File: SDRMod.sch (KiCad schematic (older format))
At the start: 46 parts, among them P1 CONN_02X06, Q1 Q_NPN_BCE, U1 AX5043, U2 74LVC125, U3 74LVC125, Y1 Crystal

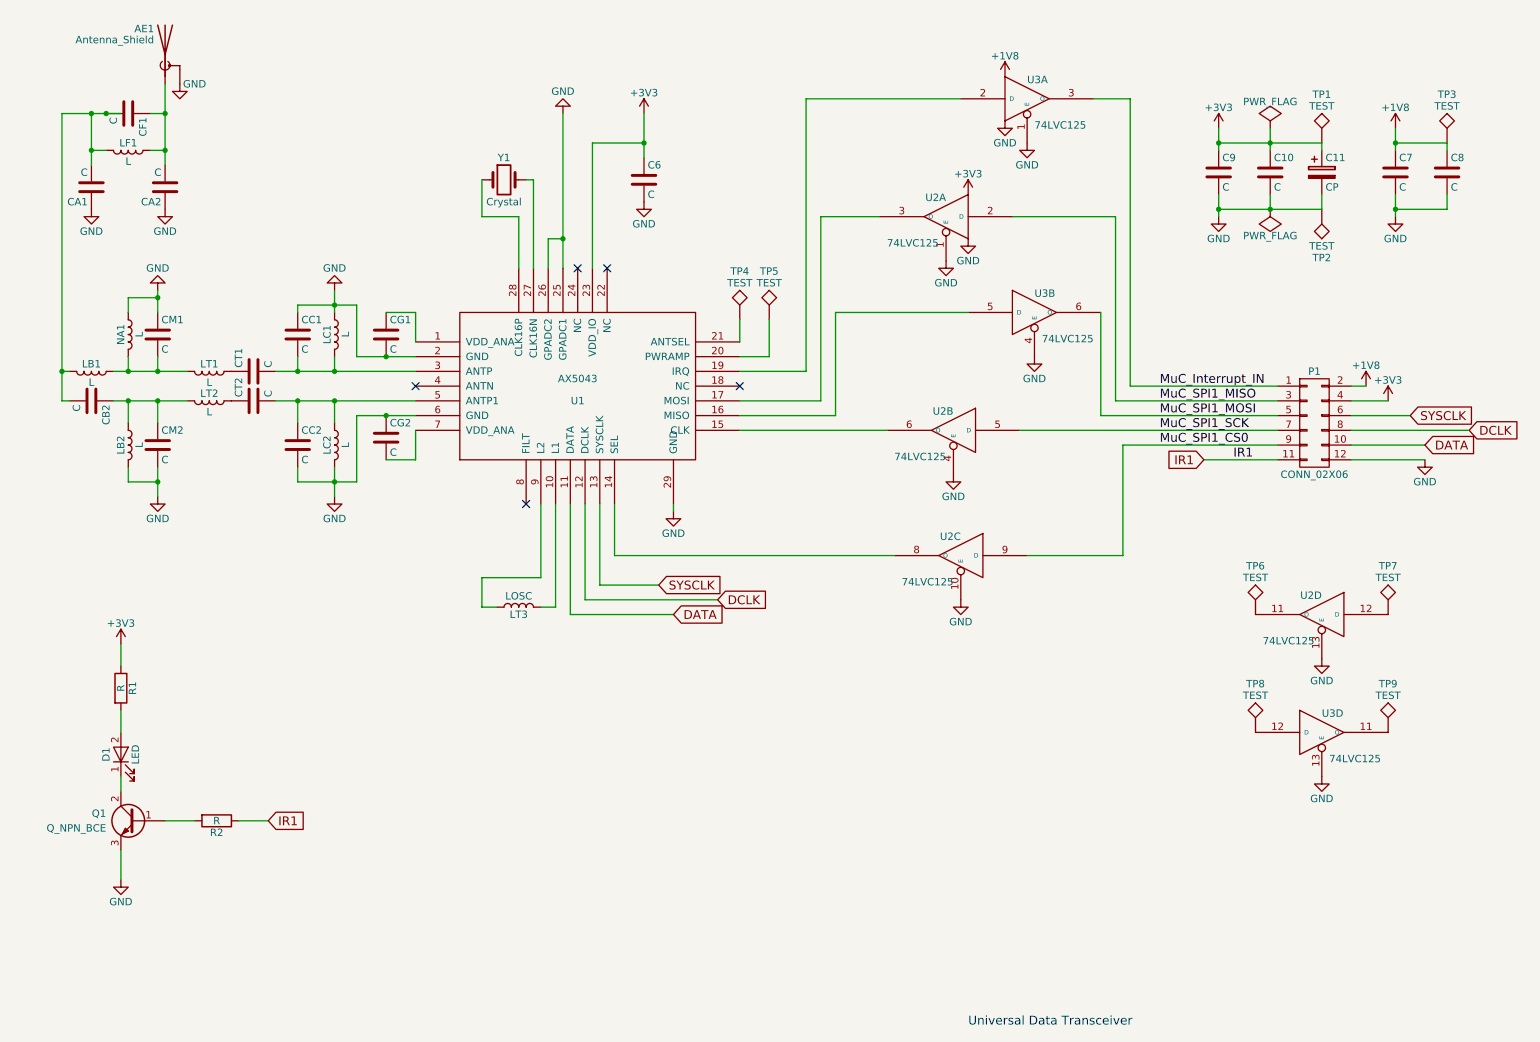
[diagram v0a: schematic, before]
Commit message: the correct project uploaded (with FET based level shifters)
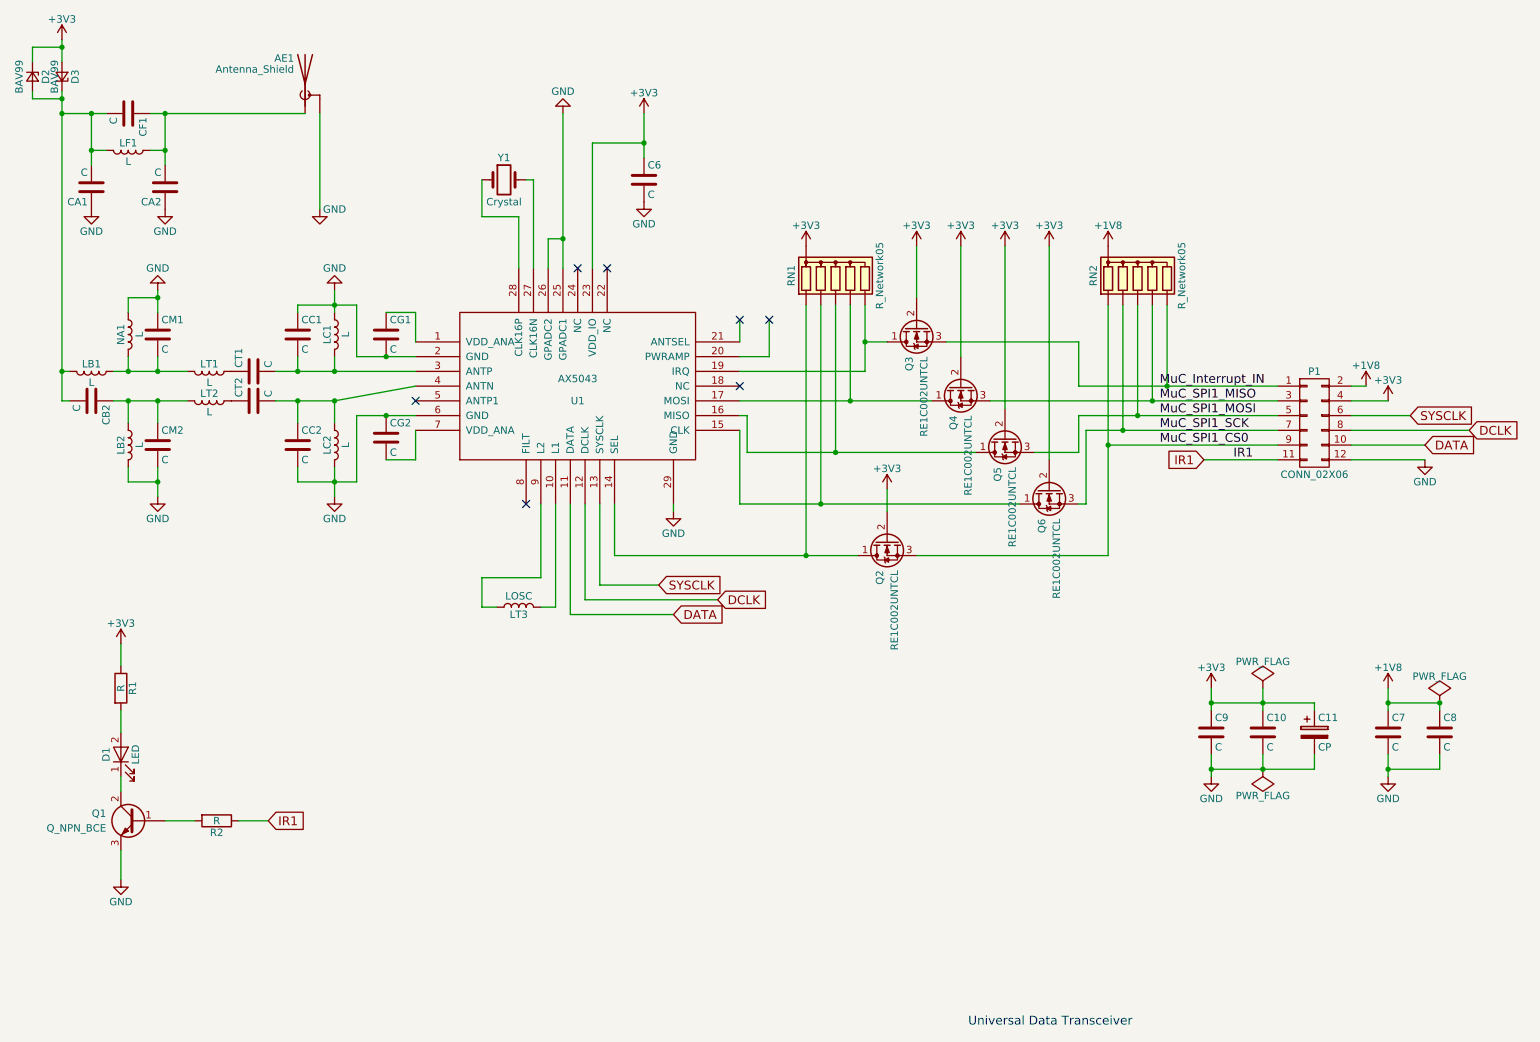
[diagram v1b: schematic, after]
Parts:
- removed TP1, TP2, TP3, TP4, TP5, TP6, TP7, TP8, TP9: TEST, Measurement_Points:Measurement_Point_Round-SMD-Pad_Small, symbol TEST
- removed U2, U3: 74LVC125, Housings_SOIC:SOIC-14_3.9x8.7mm_Pitch1.27mm, symbol 74LVC125
- added D2, D3: BAV99, Diodes_SMD:D_SCD80_HandSoldering, symbol D_Zener_Small
- added Q2, Q3, Q4, Q5, Q6: RE1C002UNTCL, TO_SOT_Packages_SMD:SOT-23_Handsoldering, symbol Q_NMOS_DGS
- added RN1, RN2: R_Network05, TO_SOT_Packages_SMD:SOT-23-6_Handsoldering, symbol R_Network05
- AE1: footprint Wire_Connections_Bridges:WireConnection_1.00mmDrill -> Connectors:SMB_Straight
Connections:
- net +1V8: now also RN2.1 (common); no longer C10.1, C11.1, C6.1, C9.1, P1.4 (P4), R1.1, U1.23 (VDD_IO)
- net MuC_Interrupt_IN: now also Q3.3 (S), RN2.6 (R5)
- net MuC_SPI1_CS0: now also Q2.3 (S), RN2.2 (R1)
- net MuC_SPI1_MISO: now also Q4.3 (S), RN2.5 (R4)
- net MuC_SPI1_MOSI: now also Q5.3 (S), RN2.4 (R3)
- net MuC_SPI1_SCK: now also Q6.3 (S), RN2.3 (R2)
- net at U1.14 (SEL): now also Q2.1 (D), RN1.2 (R1)
- net at U1.15 (CLK): now also Q6.1 (D), RN1.3 (R2)
- net at U1.16 (MISO): now also Q5.1 (D), RN1.4 (R3)
- net at U1.17 (MOSI): now also Q4.1 (D), RN1.5 (R4)
- net at U1.19 (IRQ): now also Q3.1 (D), RN1.6 (R5)
- net at U1.4 (ANTN): now also CC2.1, CT2.2, LC2.1
- net at CA1.2, CB2.2, CF1.2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: now also D2.2 (A), D3.1 (K)
- new net +3V3: C10.1, C11.1, C6.1, C9.1, D2.1 (K), D3.2 (A), P1.4 (P4), Q2.2 (G), Q3.2 (G), Q4.2 (G), Q5.2 (G), Q6.2 (G), R1.1, RN1.1 (common), U1.23 (VDD_IO)
- now unconnected: U1.5 (ANTP1)
- no-connect marks 5 -> 7
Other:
- moved on the sheet: AE1, C10, C11, C7, C8, C9
